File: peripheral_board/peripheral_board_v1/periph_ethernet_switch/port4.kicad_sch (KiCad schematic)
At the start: 0 parts

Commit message: Ethernet Switch WIP
# Changes Made

## Ports
Finished all the Ethernet ports for 1 through 5 while leaving 6 unconfigured.

## Hardware Config
Added in the strap in configuration using break out pins for ease of use and not having to worry about switches. This should allow for the built in Default config but allows for external setting as well.
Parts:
- added C44, C45, C46, C47: 0.1uF, Capacitor_SMD:C_0603_1608Metric, symbol Device:C
- added J4: 0826-1G1T-23-F, SCALES:BEL_0826-1G1T-23-F, symbol SCALES:0826-1G1T-23-F
- added R7, R8: 100, symbol Device:R_US
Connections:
- new net: C47.2, J4.1 (TRCT3)
- new net: C45.2, J4.12 (TRCT1)
- new net: J4.14, R7.1
- new net: J4.16, R8.1
- new net: C46.2, J4.6 (TRCT2)
- new net: C44.2, J4.7 (TRCT4)
- new net +3.3V: R7.2, R8.2
- new net CGND: J4.S1 (SHIELD), J4.S2 (SHIELD__1)
- new net LED4_0: J4.13
- new net LED4_1: J4.15
- new net SGND: C44.1, C45.1, C46.1, C47.1
- new net TXRX4M_A: J4.10 (TRD1-)
- new net TXRX4M_B: J4.5 (TRD2-)
- new net TXRX4M_C: J4.2 (TRD3-)
- new net TXRX4M_D: J4.9 (TRD4-)
- new net TXRX4P_A: J4.11 (TRD1+)
- new net TXRX4P_B: J4.4 (TRD2+)
- new net TXRX4P_C: J4.3 (TRD3+)
- new net TXRX4P_D: J4.8 (TRD4+)
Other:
- note added: "LEDx_1 pin indicates the link status LEDx_0 pin indicates the activity status"

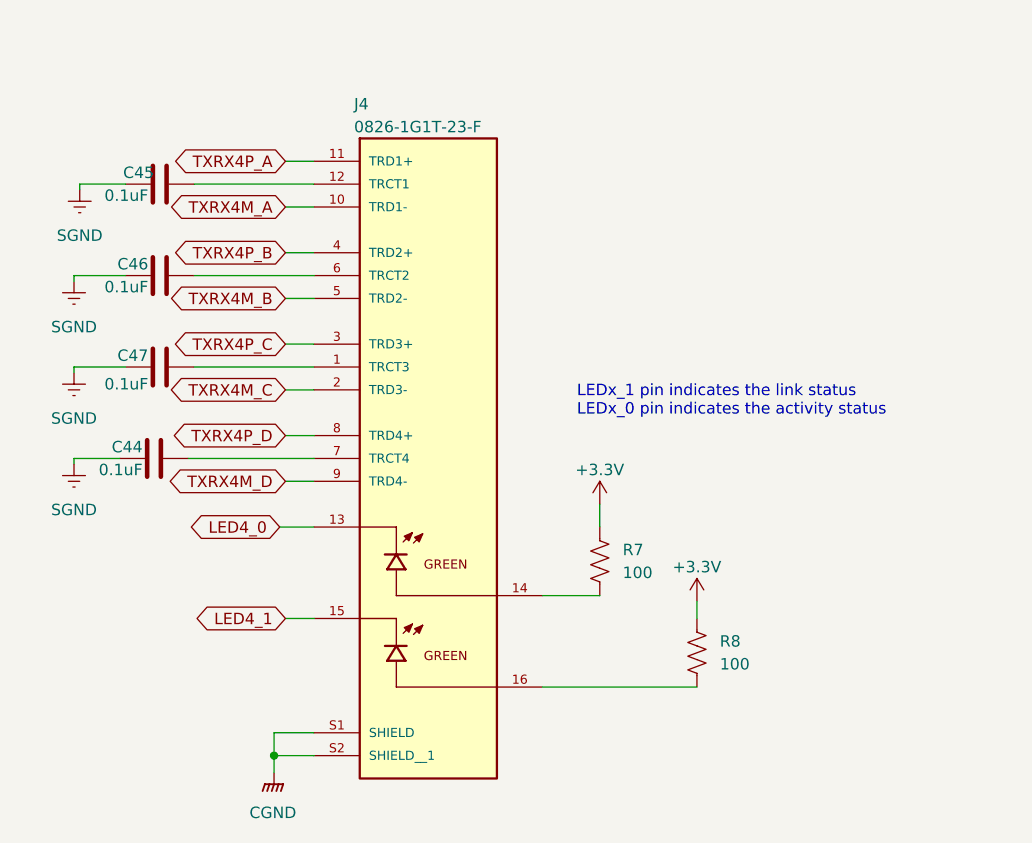
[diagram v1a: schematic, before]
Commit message: Switch update
Still making changes to the switch. Finished most of the power but still need to work on the power logic for when it is being powered. Need to do the debug and the clock logic but it is getting close to pcb design.
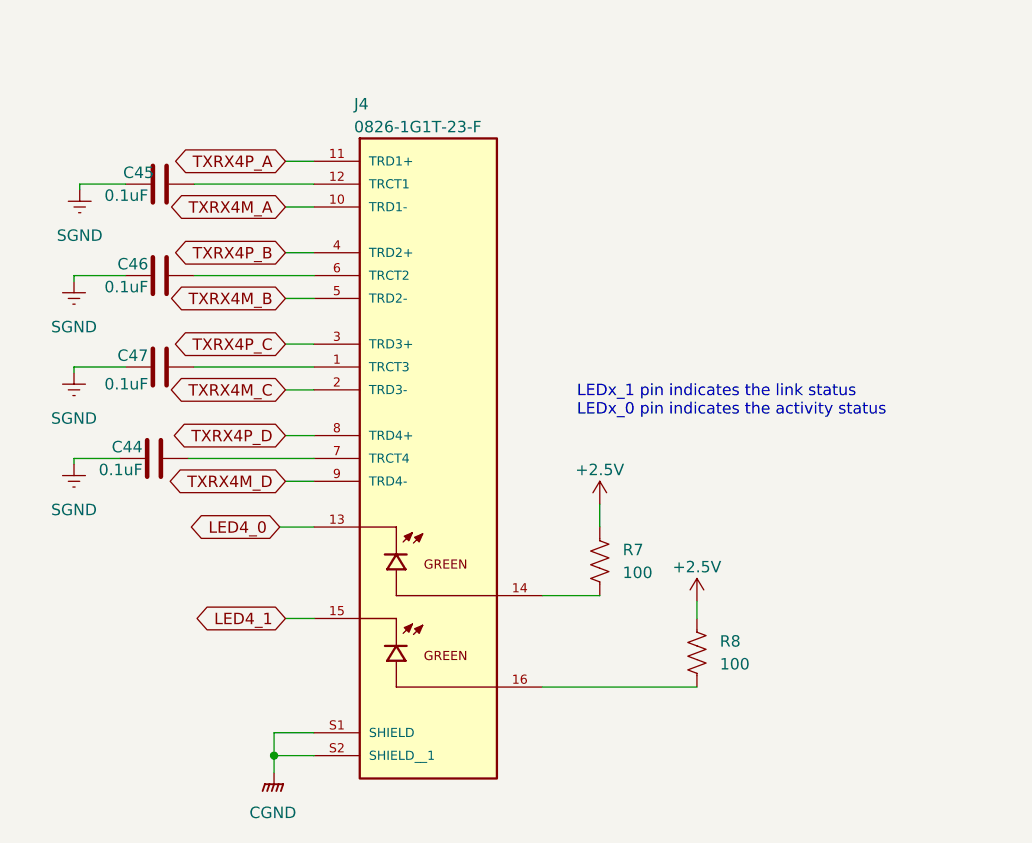
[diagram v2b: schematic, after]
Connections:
- net +3.3V renamed +2.5V
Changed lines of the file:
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@@
-	)
-	(symbol
-		(lib_id "power:+3.3V")
-		(at 78.105 66.04 0)
-		(unit 1)
-		(exclude_from_sim no)
-		(in_bom yes)
-		(on_board yes)
-		(dnp no)
-		(property "Reference" "#PWR036"
-			(at 78.105 69.85 0)
-			(effects
-				(font
-					(size 1.27 1.27)
-				)
-				(hide yes)
-			)
-		)
-		(property "Value" "+3.3V"
-			(at 78.105 62.23 0)
-			(effects
-				(font
-					(size 1.27 1.27)
-				)
-			)
-		)
-		(property "Footprint" ""
-			(at 78.105 66.04 0)
-			(effects
-				(font
-					(size 1.27 1.27)
-				)
-				(hide yes)
-			)
-		)
-		(property "Datasheet" ""
-			(at 78.105 66.04 0)
-			(effects
-				(font
-					(size 1.27 1.27)
-				)
-				(hide yes)
-			)
-		)
-		(property "Description" "Power symbol creates a global label with name \"+3.3V\""
-			(at 78.105 66.04 0)
-			(effects
-				(font
-					(size 1.27 1.27)
-				)
-				(hide yes)
-			)
-		)
-		(pin "1"
-		)
-		(instances
-			(project "periph_ethernet_switch"
-				(path "/065aff9d-de72-4d05-9bf8-aade8202d5c4/c3ca900e-99ac-4769-98db-f2b6577cf32c"
-					(reference "#PWR036")
-					(unit 1)
-				)
-			)
-		)
 	)
 	(symbol
@@
 				(path "/065aff9d-de72-4d05-9bf8-aade8202d5c4/c3ca900e-99ac-4769-98db-f2b6577cf32c"
 					(reference "C47")
+					(unit 1)
+				)
+			)
+		)
+	)
+	(symbol
+		(lib_id "power:+2V5")
+		(at 88.9 76.835 0)
+		(unit 1)
+		(exclude_from_sim no)
+		(in_bom yes)
+		(on_board yes)
+		(dnp no)
+		(property "Reference" "#PWR037"
+			(at 88.9 80.645 0)
+			(effects
+				(font
+					(size 1.27 1.27)
+				)
+				(hide yes)
+			)
+		)
+		(property "Value" "+2.5V"
+			(at 88.9 73.025 0)
+			(effects
+				(font
+					(size 1.27 1.27)
+				)
+			)
+		)
+		(property "Footprint" ""
+			(at 88.9 76.835 0)
+			(effects
+				(font
+					(size 1.27 1.27)
+				)
+				(hide yes)
+			)
+		)
+		(property "Datasheet" ""
+			(at 88.9 76.835 0)
+			(effects
+				(font
+					(size 1.27 1.27)
+				)
+				(hide yes)
+			)
+		)
+		(property "Description" "Power symbol creates a global label with name \"+2V5\""
+			(at 88.9 76.835 0)
+			(effects
+				(font
+					(size 1.27 1.27)
+				)
+				(hide yes)
+			)
+		)
+		(pin "1"
+		)
+		(instances
+			(project "periph_ethernet_switch"
+				(path "/065aff9d-de72-4d05-9bf8-aade8202d5c4/c3ca900e-99ac-4769-98db-f2b6577cf32c"
+					(reference "#PWR037")
 					(unit 1)
 				)
@@
 	)
 	(symbol
-		(lib_id "power:+3.3V")
-		(at 88.9 76.835 0)
-		(unit 1)
-		(exclude_from_sim no)
-		(in_bom yes)
-		(on_board yes)
-		(dnp no)
-		(property "Reference" "#PWR037"
-			(at 88.9 80.645 0)
-			(effects
-				(font
-					(size 1.27 1.27)
-				)
-				(hide yes)
-			)
-		)
-		(property "Value" "+3.3V"
-			(at 88.9 73.025 0)
-			(effects
-				(font
-					(size 1.27 1.27)
-				)
-			)
-		)
-		(property "Footprint" ""
-			(at 88.9 76.835 0)
+		(lib_id "power:+2V5")
+		(at 78.105 66.04 0)
+		(unit 1)
+		(exclude_from_sim no)
+		(in_bom yes)
+		(on_board yes)
+		(dnp no)
+		(property "Reference" "#PWR036"
+			(at 78.105 69.85 0)
+			(effects
+				(font
+					(size 1.27 1.27)
+				)
+				(hide yes)
+			)
+		)
+		(property "Value" "+2.5V"
+			(at 78.105 62.23 0)
+			(effects
+				(font
+					(size 1.27 1.27)
+				)
+			)
+		)
+		(property "Footprint" ""
+			(at 78.105 66.04 0)
 			(effects
 				(font
@@
 		)
 		(property "Datasheet" ""
-			(at 88.9 76.835 0)
-			(effects
-				(font
-					(size 1.27 1.27)
-				)
-				(hide yes)
-			)
-		)
-		(property "Description" "Power symbol creates a global label with name \"+3.3V\""
-			(at 88.9 76.835 0)
-			(effects
-				(font
-					(size 1.27 1.27)
-				)
-				(hide yes)
-			)
-		)
-		(pin "1"
-		)
-		(instances
-			(project "periph_ethernet_switch"
-				(path "/065aff9d-de72-4d05-9bf8-aade8202d5c4/c3ca900e-99ac-4769-98db-f2b6577cf32c"
-					(reference "#PWR037")
-					(unit 1)
-				)
+			(at 78.105 66.04 0)
+			(effects
+				(font
+					(size 1.27 1.27)
+				)
+				(hide yes)
+			)
+		)
+		(property "Description" "Power symbol creates a global label with name \"+2V5\""
+			(at 78.105 66.04 0)
+			(effects
+				(font
+					(size 1.27 1.27)
+				)
+				(hide yes)
+			)
+		)
+		(pin "1"
+		)
+		(instances
+			(project "periph_ethernet_switch"
+				(path "/065aff9d-de72-4d05-9bf8-aade8202d5c4/c3ca900e-99ac-4769-98db-f2b6577cf32c"
+					(reference "#PWR036")
+					(unit 1)
+				)

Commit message: Switch Schematic Update
The switch schematic should be done. Waiting on a review but should be ready for moving forward with board layout.
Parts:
- R7, R8: footprint (none) -> Resistor_SMD:R_0603_1608Metric
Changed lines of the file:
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@@
 			)
 		)
-		(property "Footprint" ""
+		(property "Footprint" "Resistor_SMD:R_0603_1608Metric"
 			(at 87.884 82.296 90)
 			(effects
@@
 			)
 		)
-		(property "Footprint" ""
+		(property "Footprint" "Resistor_SMD:R_0603_1608Metric"
 			(at 77.089 72.136 90)
 			(effects

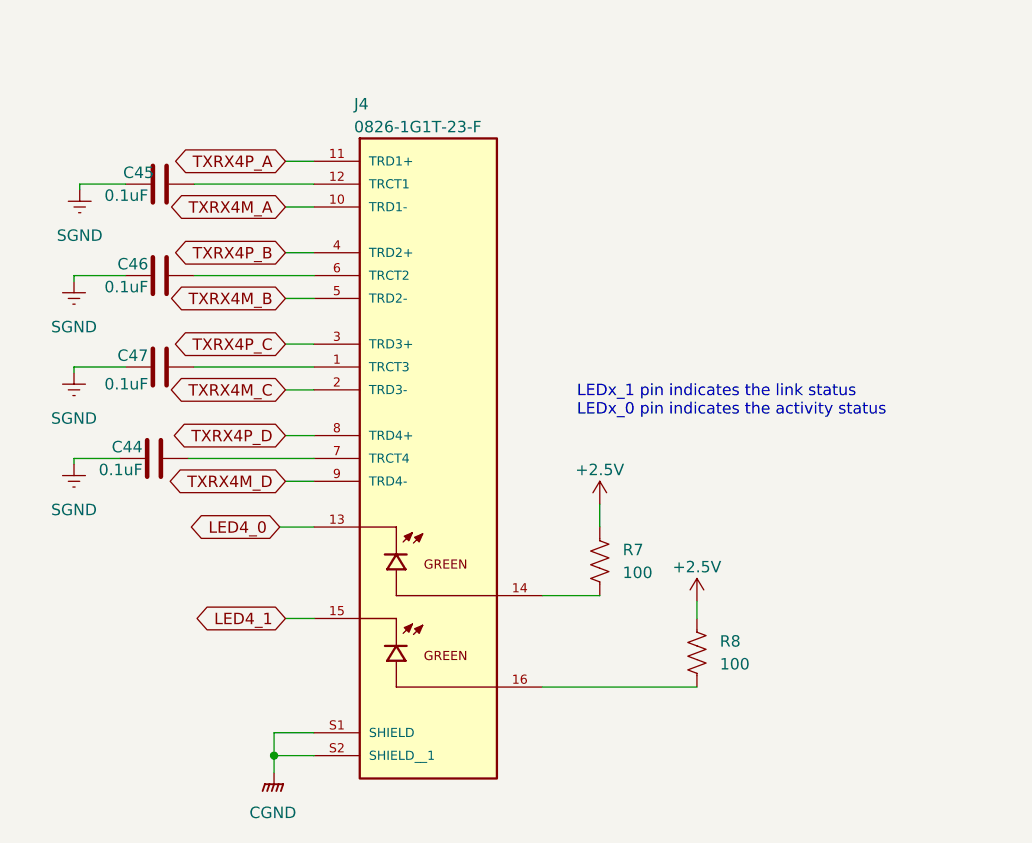
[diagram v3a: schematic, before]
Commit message: Moving to PCB layout
Finished the schematic and now working on the PCB. Got the RJ45 ports on the board but it does not look like it will fit in the current form factor.
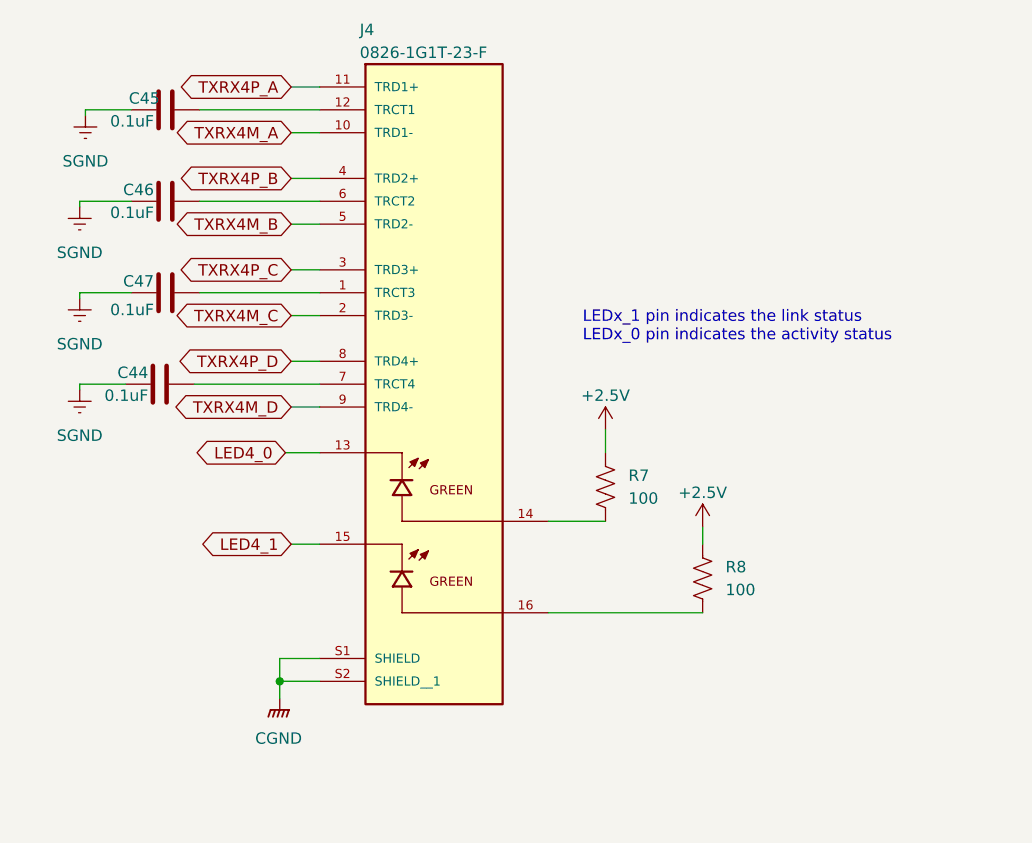
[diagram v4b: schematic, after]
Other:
- moved on the sheet: C44, C45, C46, C47, J4, R7, R8

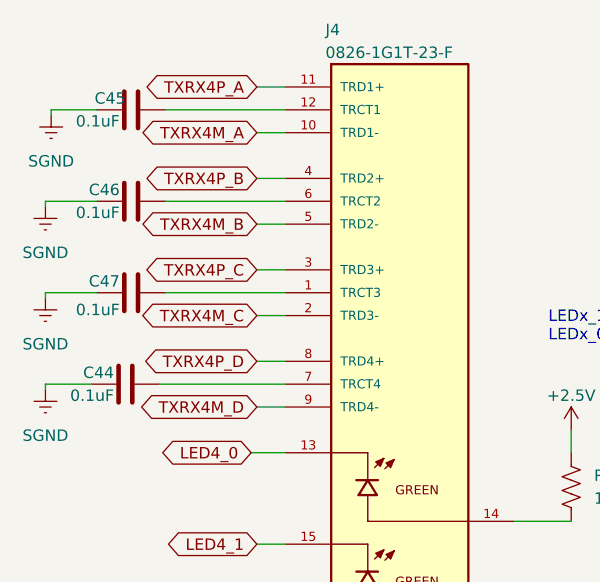
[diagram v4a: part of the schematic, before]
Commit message: Working on the board layout
The differential pairs are being a pain. Signals B and D need to be crossed which is not ideal. Some of the signals do not seem to want to connect which is making this a fun time. Still need to put in the structures like the drill holes. I have not done the capacitors yet but I think I might do that next time then do the DP routing to make life a bit more straight forward.
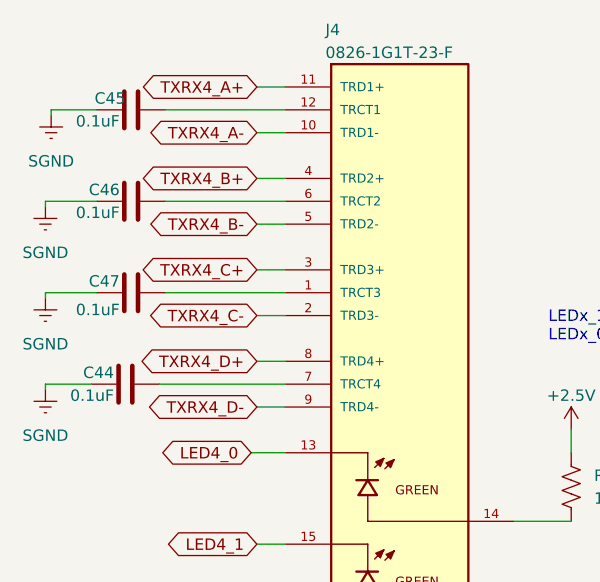
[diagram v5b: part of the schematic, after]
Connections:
- net TXRX4M_A renamed TXRX4_A-
- net TXRX4M_B renamed TXRX4_B-
- net TXRX4M_C renamed TXRX4_C-
- net TXRX4M_D renamed TXRX4_D-
- net TXRX4P_A renamed TXRX4_A+
- net TXRX4P_B renamed TXRX4_B+
- net TXRX4P_C renamed TXRX4_C+
- net TXRX4P_D renamed TXRX4_D+
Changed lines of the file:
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@@
 		)
 	)
-	(global_label "TXRX4M_C"
+	(global_label "TXRX4_C-"
 		(shape bidirectional)
 		(at 43.815 45.085 180)
@@
 		)
 		(property "Intersheetrefs" "${INTERSHEET_REFS}"
-			(at 30.1634 45.085 0)
-			(effects
-				(font
-					(size 1.27 1.27)
-				)
-				(justify right)
-				(hide yes)
-			)
-		)
-	)
-	(global_label "TXRX4P_A"
+			(at 30.0424 45.085 0)
+			(effects
+				(font
+					(size 1.27 1.27)
+				)
+				(justify right)
+				(hide yes)
+			)
+		)
+		(property "Netclass" "DP_100R_TOP"
+			(at 43.815 47.2758 0)
+			(effects
+				(font
+					(size 1.27 1.27)
+				)
+				(justify right)
+				(hide yes)
+			)
+		)
+	)
+	(global_label "TXRX4_A+"
 		(shape bidirectional)
 		(at 43.815 19.685 180)
@@
 		)
 		(property "Intersheetrefs" "${INTERSHEET_REFS}"
-			(at 30.5262 19.685 0)
-			(effects
-				(font
-					(size 1.27 1.27)
-				)
-				(justify right)
-				(hide yes)
-			)
-		)
-	)
-	(global_label "TXRX4P_C"
+			(at 30.2238 19.685 0)
+			(effects
+				(font
+					(size 1.27 1.27)
+				)
+				(justify right)
+				(hide yes)
+			)
+		)
+		(property "Netclass" "DP_100R_TOP"
+			(at 43.815 21.8758 0)
+			(effects
+				(font
+					(size 1.27 1.27)
+				)
+				(justify right)
+				(hide yes)
+			)
+		)
+	)
+	(global_label "TXRX4_C+"
 		(shape bidirectional)
 		(at 43.815 40.005 180)
@@
 		)
 		(property "Intersheetrefs" "${INTERSHEET_REFS}"
-			(at 30.3448 40.005 0)
-			(effects
-				(font
-					(size 1.27 1.27)
-				)
-				(justify right)
-				(hide yes)
-			)
-		)
-	)
-	(global_label "TXRX4M_D"
+			(at 30.0424 40.005 0)
+			(effects
+				(font
+					(size 1.27 1.27)
+				)
+				(justify right)
+				(hide yes)
+			)
+		)
+		(property "Netclass" "DP_100R_TOP"
+			(at 43.815 42.1958 0)
+			(effects
+				(font
+					(size 1.27 1.27)
+				)
+				(justify right)
+				(hide yes)
+			)
+		)
+	)
+	(global_label "TXRX4_D-"
 		(shape bidirectional)
 		(at 43.815 55.245 180)
@@
 		)
 		(property "Intersheetrefs" "${INTERSHEET_REFS}"
-			(at 30.1634 55.245 0)
-			(effects
-				(font
-					(size 1.27 1.27)
-				)
-				(justify right)
-				(hide yes)
-			)
-		)
-	)
-	(global_label "TXRX4P_D"
+			(at 30.0424 55.245 0)
+			(effects
+				(font
+					(size 1.27 1.27)
+				)
+				(justify right)
+				(hide yes)
+			)
+		)
+		(property "Netclass" "DP_100R_TOP"
+			(at 43.815 57.4358 0)
+			(effects
+				(font
+					(size 1.27 1.27)
+				)
+				(justify right)
+				(hide yes)
+			)
+		)
+	)
+	(global_label "TXRX4_D+"
 		(shape bidirectional)
 		(at 43.815 50.165 180)
@@
 		)
 		(property "Intersheetrefs" "${INTERSHEET_REFS}"
-			(at 30.3448 50.165 0)
+			(at 30.0424 50.165 0)
+			(effects
+				(font
+					(size 1.27 1.27)
+				)
+				(justify right)
+				(hide yes)
+			)
+		)
+		(property "Netclass" "DP_100R_TOP"
+			(at 43.815 52.3558 0)
 			(effects
 				(font
@@
 		)
 	)
-	(global_label "TXRX4P_B"
+	(global_label "TXRX4_B+"
 		(shape bidirectional)
 		(at 43.815 29.845 180)
@@
 		)
 		(property "Intersheetrefs" "${INTERSHEET_REFS}"
-			(at 30.3448 29.845 0)
+			(at 30.0424 29.845 0)
+			(effects
+				(font
+					(size 1.27 1.27)
+				)
+				(justify right)
+				(hide yes)
+			)
+		)
+		(property "Netclass" "DP_100R_TOP"
+			(at 43.815 32.0358 0)
 			(effects
 				(font
@@
 		)
 	)
-	(global_label "TXRX4M_B"
+	(global_label "TXRX4_B-"
 		(shape bidirectional)
 		(at 43.815 34.925 180)
@@
 		)
 		(property "Intersheetrefs" "${INTERSHEET_REFS}"
-			(at 30.1634 34.925 0)
-			(effects
-				(font
-					(size 1.27 1.27)
-				)
-				(justify right)
-				(hide yes)
-			)
-		)
-	)
-	(global_label "TXRX4M_A"
+			(at 30.0424 34.925 0)
+			(effects
+				(font
+					(size 1.27 1.27)
+				)
+				(justify right)
+				(hide yes)
+			)
+		)
+		(property "Netclass" "DP_100R_TOP"
+			(at 43.815 37.1158 0)
+			(effects
+				(font
+					(size 1.27 1.27)
+				)
+				(justify right)
+				(hide yes)
+			)
+		)
+	)
+	(global_label "TXRX4_A-"
 		(shape bidirectional)
 		(at 43.815 24.765 180)
@@
 		)
 		(property "Intersheetrefs" "${INTERSHEET_REFS}"
-			(at 30.3448 24.765 0)
-			(effects
-				(font
+			(at 30.2238 24.765 0)
+			(effects
+				(font
+					(size 1.27 1.27)
+				)
+				(justify right)
+				(hide yes)
+			)
+		)
+		(property "Netclass" "DP_100R_TOP"
+			(at 43.815 26.9558 0)
+			(effects
+				(font
